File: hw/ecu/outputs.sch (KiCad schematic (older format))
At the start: 44 parts, among them J12 VALVE_REG, J13 OUTPUTS, J14 VALVES_FRONT, J15 VALVES_BACK, Q1 IPD30N06S4L23, Q2 IPD30N06S4L23, Q3 DMP2035, Q4 IPD30N06S4L23, Q5 IPD30N06S4L23, U8 TSV912

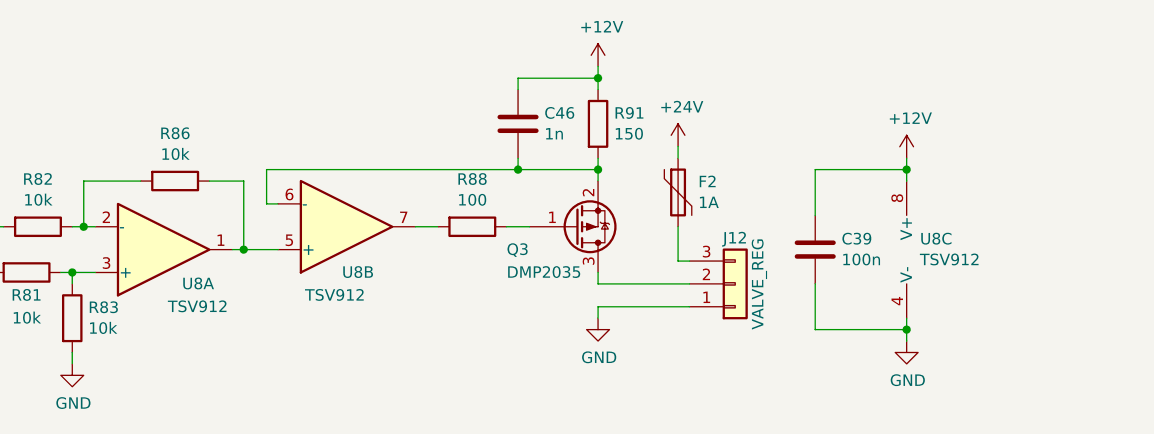
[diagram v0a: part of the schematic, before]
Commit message: Fixed opamp on ecu board to one with correct power range
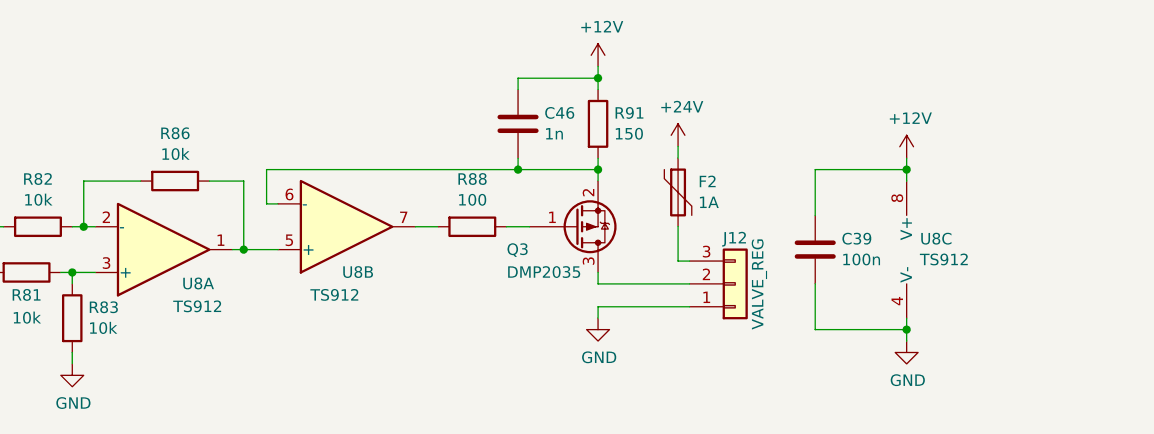
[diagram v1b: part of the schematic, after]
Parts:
- U8: value TSV912 -> TS912
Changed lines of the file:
@@
 Wire Wire Line
 	5150 6950 5200 6950
-$Comp
-L Amplifier_Operational:TSV912IDT U?
-U 1 1 61A2F93D
-P 2900 6900
-AR Path="/61A2F93D" Ref="U?"  Part="1"
-AR Path="/61A01E90/61A2F93D" Ref="U8"  Part="1"
-F 0 "U8" H 3050 7050 50  0000 C CNN
-F 1 "TSV912" H 3050 7150 50  0000 C CNN
-F 2 "Package_SO:SOIC-8_3.9x4.9mm_P1.27mm" H 2900 6900 50  0001 C CNN
-F 3 "www.st.com/resource/en/datasheet/tsv911.pdf" H 2900 6900 50  0001 C CNN
-	1    2900 6900
-	1    0    0    1
-$EndComp
-$Comp
-L Amplifier_Operational:TSV912IDT U?
-U 2 1 61A2F944
-P 3700 6800
-AR Path="/61A2F944" Ref="U?"  Part="2"
-AR Path="/61A01E90/61A2F944" Ref="U8"  Part="2"
-F 0 "U8" H 3750 7000 50  0000 C CNN
-F 1 "TSV912" H 3650 7100 50  0000 C CNN
-F 2 "Package_SO:SOIC-8_3.9x4.9mm_P1.27mm" H 3700 6800 50  0001 C CNN
-F 3 "www.st.com/resource/en/datasheet/tsv911.pdf" H 3700 6800 50  0001 C CNN
-	2    3700 6800
-	1    0    0    1
-$EndComp
 Wire Wire Line
 	2500 7000 2600 7000
@@
 AR Path="/61A01E90/61C396EC" Ref="U8"  Part="3"
 F 0 "U8" H 6208 6946 50  0000 L CNN
-F 1 "TSV912" H 6208 6855 50  0000 L CNN
+F 1 "TS912" H 6208 6855 50  0000 L CNN
 F 2 "Package_SO:SOIC-8_3.9x4.9mm_P1.27mm" H 6250 6900 50  0001 C CNN
 F 3 "www.st.com/resource/en/datasheet/tsv911.pdf" H 6250 6900 50  0001 C CNN
@@
 Wire Wire Line
 	4450 6550 3350 6550
+$Comp
+L Amplifier_Operational:TSV912IDT U?
+U 2 1 61A2F944
+P 3700 6800
+AR Path="/61A2F944" Ref="U?"  Part="2"
+AR Path="/61A01E90/61A2F944" Ref="U8"  Part="2"
+F 0 "U8" H 3750 7000 50  0000 C CNN
+F 1 "TS912" H 3650 7100 50  0000 C CNN
+F 2 "Package_SO:SOIC-8_3.9x4.9mm_P1.27mm" H 3700 6800 50  0001 C CNN
+F 3 "www.st.com/resource/en/datasheet/tsv911.pdf" H 3700 6800 50  0001 C CNN
+	2    3700 6800
+	1    0    0    1
+$EndComp
+$Comp
+L Amplifier_Operational:TSV912IDT U?
+U 1 1 61A2F93D
+P 2900 6900
+AR Path="/61A2F93D" Ref="U?"  Part="1"
+AR Path="/61A01E90/61A2F93D" Ref="U8"  Part="1"
+F 0 "U8" H 3050 7050 50  0000 C CNN
+F 1 "TS912" H 3050 7150 50  0000 C CNN
+F 2 "Package_SO:SOIC-8_3.9x4.9mm_P1.27mm" H 2900 6900 50  0001 C CNN
+F 3 "www.st.com/resource/en/datasheet/tsv911.pdf" H 2900 6900 50  0001 C CNN
+	1    2900 6900
+	1    0    0    1
+$EndComp
 $EndSCHEMATC
